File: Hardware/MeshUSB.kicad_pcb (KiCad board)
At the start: 2 copper layers, 30.2 x 44.3 mm, 42 parts, among them P1 USB_4, P2 PVCell, Q1 MOS_P, U1 XBEE, U2 AP7313-3.3VREGULATOR, U4 FT231X-SSOP, U5 LTC4070

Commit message: Begin major modifications for post v0.2.
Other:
- board text added: "MeshUSBv0.3"
- board text removed: "MeshUSBv0.2"

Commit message: Begin Layout. Still some schematic additions required.
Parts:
- removed C1: 10uF, _MUSB_SM0603_Capa
- removed D3, D4: DIODE-NC, SOT23
- removed R3, R6: 22R, _MUSB_SM0603_Resistor
- added C30: 100n, _MUSB_:_MUSB_SM0603_Capa, F.Cu at (165.3, 137.1)
- added D30: BAT54C, SMD_Packages:SOT23, F.Cu at (170.4, 133.4)
- added R30: 10R, _MUSB_:_MUSB_SM0603_Resistor, F.Cu at (170.0, 128.6)
- moved G0 6.98 mm to (138.5, 93.7)
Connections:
- D7 pad 1: N-0000032 -> Net-(C30-Pad1)
- Li-Battery1 pad 1: N-0000032 -> Net-(C30-Pad1)
- Q1 pad 2: N-0000032 -> Net-(C30-Pad1)
- U5 pad 2: N-0000032 -> Net-(C30-Pad1)
- U5 pad 3: N-0000032 -> Net-(U5-Pad3)
- U5 pad 8: N-0000032 -> Net-(C30-Pad1)
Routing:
- net GND: track 112.3 -> 0.00 mm, vias 3 -> 0
- net N-0000032: track 78.6 -> 0.00 mm, vias 3 -> 0
- net USB_VDD: track 45.6 -> 0.00 mm
- net Net-(D2-Pad2): track 39.7 -> 0.00 mm, vias 2 -> 0
- net _MT_PF2: track 33.1 -> 0.00 mm, vias 2 -> 0
- net Net-(P1-Pad3): track 31.1 -> 0.00 mm, vias 2 -> 0
- net Net-(H1-Pad3): track 28.0 -> 0.00 mm, vias 2 -> 0
- net Net-(D1-Pad2): track 27.9 -> 0.00 mm
- net _MT_PF3: track 27.1 -> 0.00 mm, vias 2 -> 0
- net Net-(P1-Pad2): track 20.0 -> 0.00 mm
- net Net-(H1-Pad2): track 17.4 -> 0.00 mm
- net VCCIO: track 17.3 -> 0.00 mm
- net BAT+: track 16.5 -> 0.00 mm
- net N-0000035: track 16.4 -> 0.00 mm
- net Net-(R1-Pad2): track 15.2 -> 0.00 mm
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
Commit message: Further changes. Still looking for appropriate diode and PMOS packages.
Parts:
- moved R30 29.4 mm to (143.2, 116.6), turned to 180 degrees
- moved D30 26.8 mm to (154.0, 112.2)
- moved C30 25.0 mm to (153.9, 114.9), turned to 180 degrees
- moved U2 5.89 mm to (143.4, 108.0)
- moved R4 3.10 mm to (149.2, 109.0)
- moved JP2 2.05 mm to (146.4, 108.3), turned to 0 degrees
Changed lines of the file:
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@@
   )
   (module SOT23 (layer F.Cu)
-    (at 148.5 110.88 180)
+    (at 143.36 108 180)
     (tags SOT23)
     (fp_text reference U2 (at 1.99898 -0.09906 270) (layer F.SilkS)
@@
   )
   (module _MUSB_SM0603_Resistor (layer F.Cu)
-    (at 146.07 109.09 90)
+    (at 149.17 109.04 90)
     (attr smd)
     (fp_text reference R4 (at -0.762 0 180) (layer F.SilkS)
@@
   )
   (module _MUSB_SMTJumper (layer F.Cu)
-    (at 148.5 108.32 180)
-    (attr smd)
-    (fp_text reference JP2 (at -0.74 0 270) (layer F.SilkS)
+    (at 146.45 108.28)
+    (attr smd)
+    (fp_text reference JP2 (at -0.74 0 90) (layer F.SilkS)
       (effects (font (size 0.2 0.2) (thickness 0.05)))
     )
-    (fp_text value JUMPER (at 0 0 180) (layer F.SilkS) hide
+    (fp_text value JUMPER (at 0 0) (layer F.SilkS) hide
       (effects (font (size 0.508 0.4572) (thickness 0.1143)))
     )
-    (pad 1 smd rect (at -0.65 0 180) (size 0.5 0.9) (layers F.Cu F.Paste F.Mask)
+    (pad 1 smd rect (at -0.65 0) (size 0.5 0.9) (layers F.Cu F.Paste F.Mask)
       (net 32 "Net-(JP2-Pad1)"))
-    (pad 2 smd rect (at 0.65 0 180) (size 0.5 0.9) (layers F.Cu F.Paste F.Mask)
+    (pad 2 smd rect (at 0.65 0) (size 0.5 0.9) (layers F.Cu F.Paste F.Mask)
       (net 33 "Net-(JP2-Pad2)"))
-    (pad 2 smd rect (at 0 0 180) (size 1.5 0.2032) (layers F.Cu F.Paste F.Mask)
+    (pad 2 smd rect (at 0 0) (size 1.5 0.2032) (layers F.Cu F.Paste F.Mask)
       (net 33 "Net-(JP2-Pad2)"))
     (model smd\resistors\R0603.wrl
@@
   )
   (module _MUSB_:_MUSB_SM0603_Capa (layer F.Cu)
-    (at 165.35 137.13)
-    (attr smd)
-    (fp_text reference C30 (at -0.8 0 90) (layer F.SilkS)
-      (effects (font (size 0.35 0.35) (thickness 0.0875)))
-    )
-    (fp_text value 100n (at 0.8 0 90) (layer F.SilkS)
-      (effects (font (size 0.35 0.35) (thickness 0.0875)))
-    )
-    (fp_text user "" (at -0.8 0 90) (layer F.SilkS)
+    (at 153.88 114.93 180)
+    (attr smd)
+    (fp_text reference C30 (at -0.8 0 270) (layer F.SilkS)
+      (effects (font (size 0.35 0.35) (thickness 0.0875)))
+    )
+    (fp_text value 100n (at 0.8 0 270) (layer F.SilkS)
+      (effects (font (size 0.35 0.35) (thickness 0.0875)))
+    )
+    (fp_text user "" (at -0.8 0 270) (layer F.SilkS)
       (effects (font (size 0.35 0.35) (thickness 0.0875)))
     )
@@
     (fp_line (start 1.19888 -0.635) (end 1.19888 0.635) (layer F.SilkS) (width 0.11938))
     (fp_line (start -1.19888 0.635) (end -1.19888 -0.635) (layer F.SilkS) (width 0.11938))
-    (pad 1 smd rect (at -0.762 0) (size 0.635 1.143) (layers F.Cu F.Paste F.Mask)
+    (pad 1 smd rect (at -0.762 0 180) (size 0.635 1.143) (layers F.Cu F.Paste F.Mask)
       (net 3 "Net-(C30-Pad1)"))
-    (pad 2 smd rect (at 0.762 0) (size 0.635 1.143) (layers F.Cu F.Paste F.Mask)
+    (pad 2 smd rect (at 0.762 0 180) (size 0.635 1.143) (layers F.Cu F.Paste F.Mask)
       (net 2 GND))
     (model smd\capacitors\C0603.wrl
@@
   )
   (module SMD_Packages:SOT23 (layer F.Cu)
-    (at 170.38 133.44)
+    (at 154 112.22)
     (tags SOT23)
     (fp_text reference D30 (at 1.99898 -0.09906 90) (layer F.SilkS)
@@
   )
   (module _MUSB_:_MUSB_SM0603_Resistor (layer F.Cu)
-    (at 170.04 128.64)
-    (attr smd)
-    (fp_text reference R30 (at -0.762 0 90) (layer F.SilkS)
-      (effects (font (size 0.35 0.35) (thickness 0.0875)))
-    )
-    (fp_text value 10R (at 0.762 0 90) (layer F.SilkS)
+    (at 143.16 116.63 180)
+    (attr smd)
+    (fp_text reference R30 (at -0.762 0 270) (layer F.SilkS)
+      (effects (font (size 0.35 0.35) (thickness 0.0875)))
+    )
+    (fp_text value 10R (at 0.762 0 270) (layer F.SilkS)
       (effects (font (size 0.35 0.35) (thickness 0.0875)))
     )
@@
     (fp_line (start 1.2065 -0.6985) (end 1.2065 0.6985) (layer F.SilkS) (width 0.127))
     (fp_line (start 1.2065 0.6985) (end 0.50038 0.6985) (layer F.SilkS) (width 0.127))
-    (pad 1 smd rect (at -0.762 0) (size 0.635 1.143) (layers F.Cu F.Paste F.Mask)
+    (pad 1 smd rect (at -0.762 0 180) (size 0.635 1.143) (layers F.Cu F.Paste F.Mask)
       (net 11 "Net-(D30-Pad3)"))
-    (pad 2 smd rect (at 0.762 0) (size 0.635 1.143) (layers F.Cu F.Paste F.Mask)
+    (pad 2 smd rect (at 0.762 0 180) (size 0.635 1.143) (layers F.Cu F.Paste F.Mask)
       (net 3 "Net-(C30-Pad1)"))
     (model smd\resistors\R0603.wrl
@@
     (effects (font (size 0.5 0.5) (thickness 0.125)))
   )
-  (gr_text "V.Div.\nJPR" (at 148.5 106.84) (layer F.SilkS)
+  (gr_text "V.Div.\nJPR" (at 146.38 107.02) (layer F.SilkS)
     (effects (font (size 0.45 0.45) (thickness 0.1125)))
   )

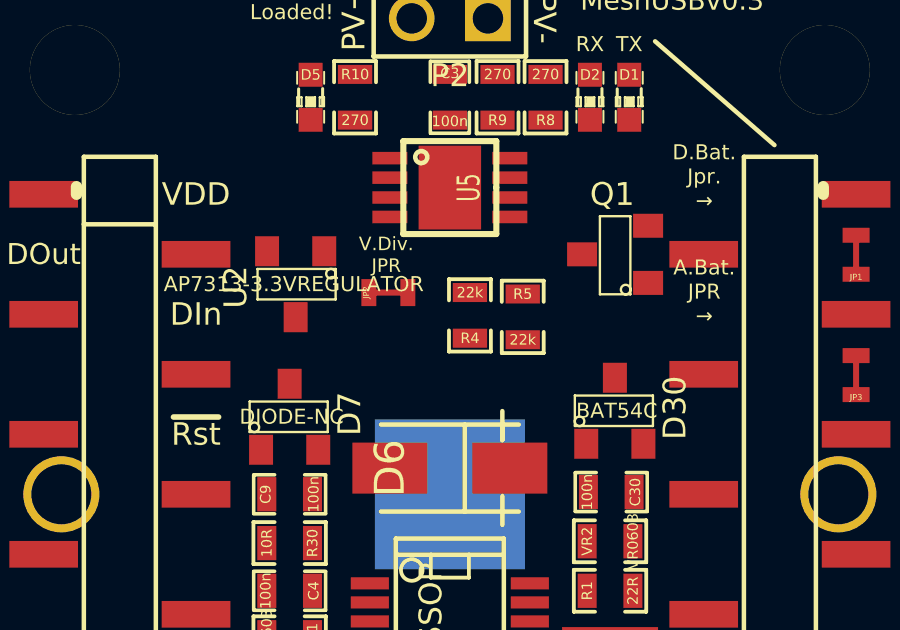
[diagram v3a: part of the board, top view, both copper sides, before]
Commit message: Schematic notes and library updates.
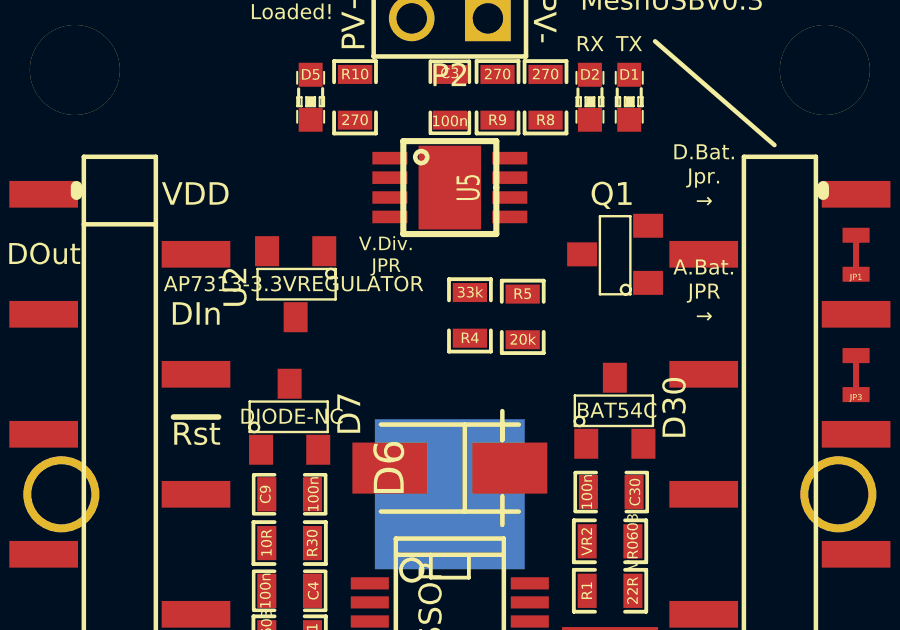
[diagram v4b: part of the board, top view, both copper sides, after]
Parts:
- removed JP2: JUMPER, _MUSB_SMTJumper
- R4: value 22k -> 33k
- R5: value 22k -> 20k
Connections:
- Q1 pad 3: Net-(JP2-Pad1) -> Net-(Q1-Pad3)
- R4 pad 2: Net-(JP2-Pad2) -> Net-(Q1-Pad3)
- R5 pad 2: GND -> _MT_PE4
- U2 pad 1: Net-(JP2-Pad1) -> Net-(Q1-Pad3)

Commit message: Almost to layout. Charging slightly modified, confirming BOM.
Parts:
- added JP2: CONN_TH_JMPR_DEFAULTCLOSED, _MUSB_SMTJumper, F.Cu at (169.8, 116.0)
- added Q2: MOS_P-INFINEON-BSS83P, SMD_Packages:SOT23, F.Cu at (146.8, 109.7)
- D30: value BAT54C -> DUAL_SHOTTKEY_PACKAGE
- R30: value 10R -> 16R; footprint _MUSB_:_MUSB_SM0603_Resistor -> SMD_Packages:SM2512
- moved R30 25.7 mm to (148.1, 91.4), turned to 0 degrees
- moved R5 7.28 mm to (156.6, 104.5), turned to 0 degrees
- moved R4 6.61 mm to (153.9, 104.4), turned to 180 degrees
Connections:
- H1 pad 5: Net-(C9-Pad1) -> Net-(H1-Pad5)

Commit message: Layoutsplosion.
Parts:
- added JP4: JUMPER, _MUSB_:_MUSB_SMTJumper, F.Cu at (162.1, 122.9)
- added P30: JST_2, _MUSB_:_MUSB_JST-2mm-THs, F.Cu at (148.5, 100.0)
- JP2: footprint _MUSB_SMTJumper -> _MUSB_:_MUSB_TH-Jumper_Default-Connected
- U1: footprint _MUSB_XBee_Board_OUTLINE_ONLY -> _MUSB_:_MUSB_XBee_Board_OUTLINE_ONLY
- moved R4 34.3 mm to (168.9, 135.3), turned to 90 degrees
- moved R5 33.8 mm to (170.4, 135.3), turned to 90 degrees
- moved JP2 30.4 mm to (141.0, 125.7)
- moved D2 27.8 mm to (143.1, 127.7), turned to 90 degrees
- moved R9 26.5 mm to (144.7, 127.8), turned to 270 degrees
- moved R8 26.0 mm to (152.2, 127.8), turned to 270 degrees
- moved D1 26.0 mm to (153.7, 127.8), turned to 90 degrees
- moved G1 20.6 mm to (169.0, 130.0)
- moved C3 17.2 mm to (156.4, 117.0), turned to 90 degrees
- moved R30 12.6 mm to (148.5, 104.0), turned to 180 degrees
- moved F1 7.64 mm to (148.5, 127.8), turned to 0 degrees
- moved P2 7.07 mm to (155.5, 100.0), turned to 0 degrees
- moved U5 6.72 mm to (148.5, 111.5)
- moved Q1 5.09 mm to (154.0, 112.1), turned to 0 degrees
- moved D30 4.12 mm to (154.0, 108.1), turned to 180 degrees
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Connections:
- JP2 pad 2: (no net) -> Net-(H1-Pad5)
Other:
- board text added: "PE4 JPR"
- board text added: "©BobPowers 2014 OpenHardware Under TAPR OHL tapr.org/OHL"
- board text removed: "V.Div. JPR"
- board text removed: "©BobPowers 2013 OpenHardware Under TAPR OHL tapr.org/OHL"

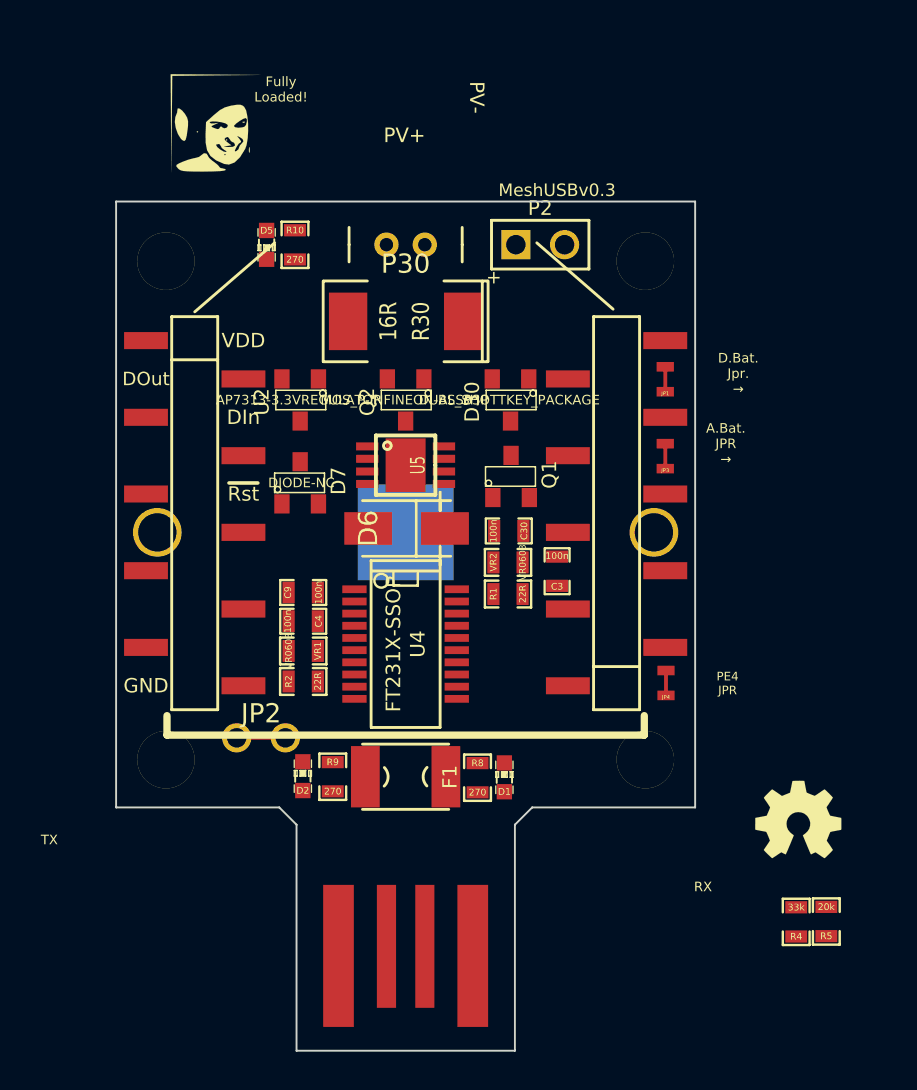
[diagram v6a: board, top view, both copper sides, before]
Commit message: Layout positions nearly finalized.
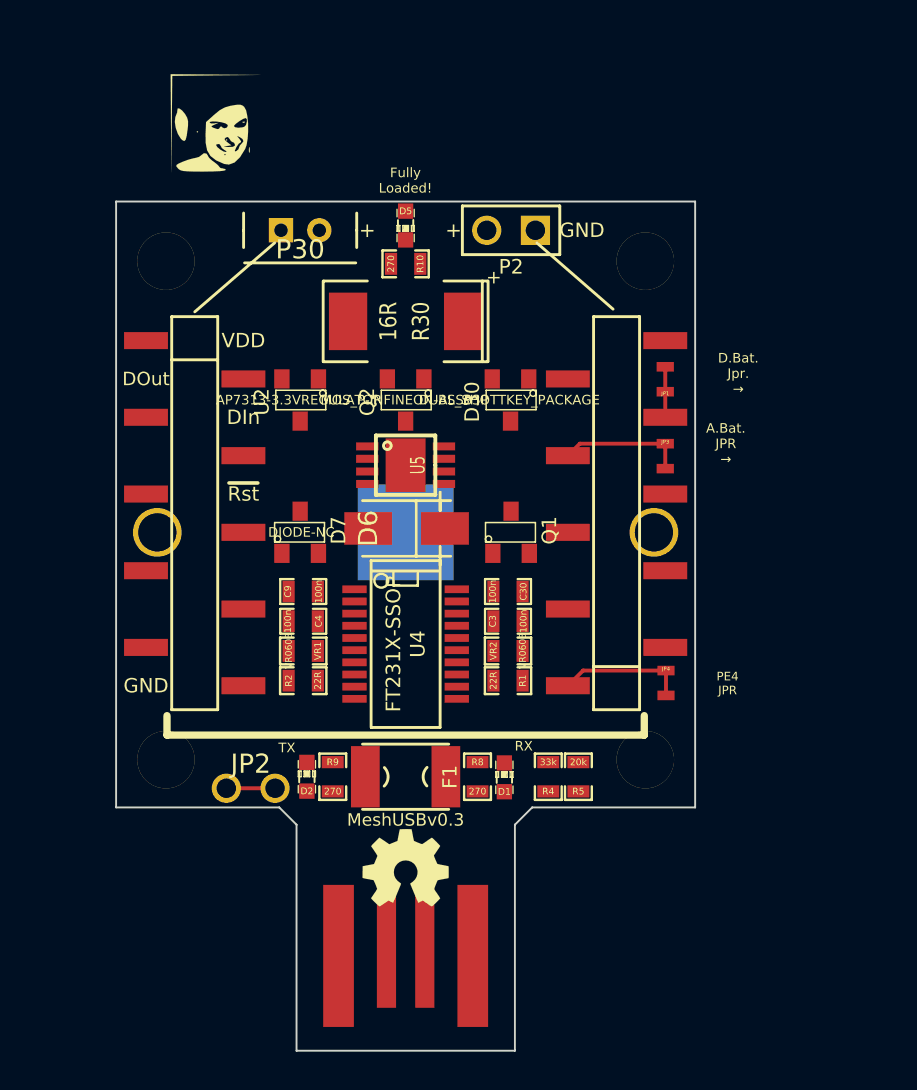
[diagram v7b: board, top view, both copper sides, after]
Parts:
- 1PIN4: footprint _MUSB_3mmTH-1pin -> _MUSB_:_MUSB_3mmTH-1pin
- moved G1 20.6 mm to (148.5, 132.5)
- moved R4 15.0 mm to (155.9, 127.8)
- moved R5 15.0 mm to (157.5, 127.8)
- moved D5 7.32 mm to (148.5, 99.0)
- moved R10 5.85 mm to (148.5, 101.0), turned to 180 degrees
- moved P30 5.55 mm to (143.0, 99.2)
- moved VR2 4.62 mm to (153.8, 121.2)
- moved R1 4.52 mm to (153.8, 122.7), turned to 180 degrees
- moved C3 3.66 mm to (153.8, 119.6), turned to 0 degrees
- moved C30 3.16 mm to (153.8, 118.1)
- moved Q1 2.91 mm to (154.0, 115.0)
- moved JP2 2.68 mm to (140.4, 128.3)
- moved D7 2.58 mm to (143.0, 115.0)
- moved P2 1.69 mm to (154.0, 99.2), turned to 180 degrees
- moved 1PIN4 0.22 mm to (161.0, 126.9)
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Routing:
- net Net-(H2-Pad1): track 0.00 -> 5.45 mm
- net Net-(H2-Pad7): track 0.00 -> 5.34 mm
- net _MT_PF2: track 0.00 -> 1.33 mm
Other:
- board text added: "+"
- board text removed: "PV+"
- board text removed: "PV-"

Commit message: Further placements, silks, refs. Next:Double check all pins and packages.
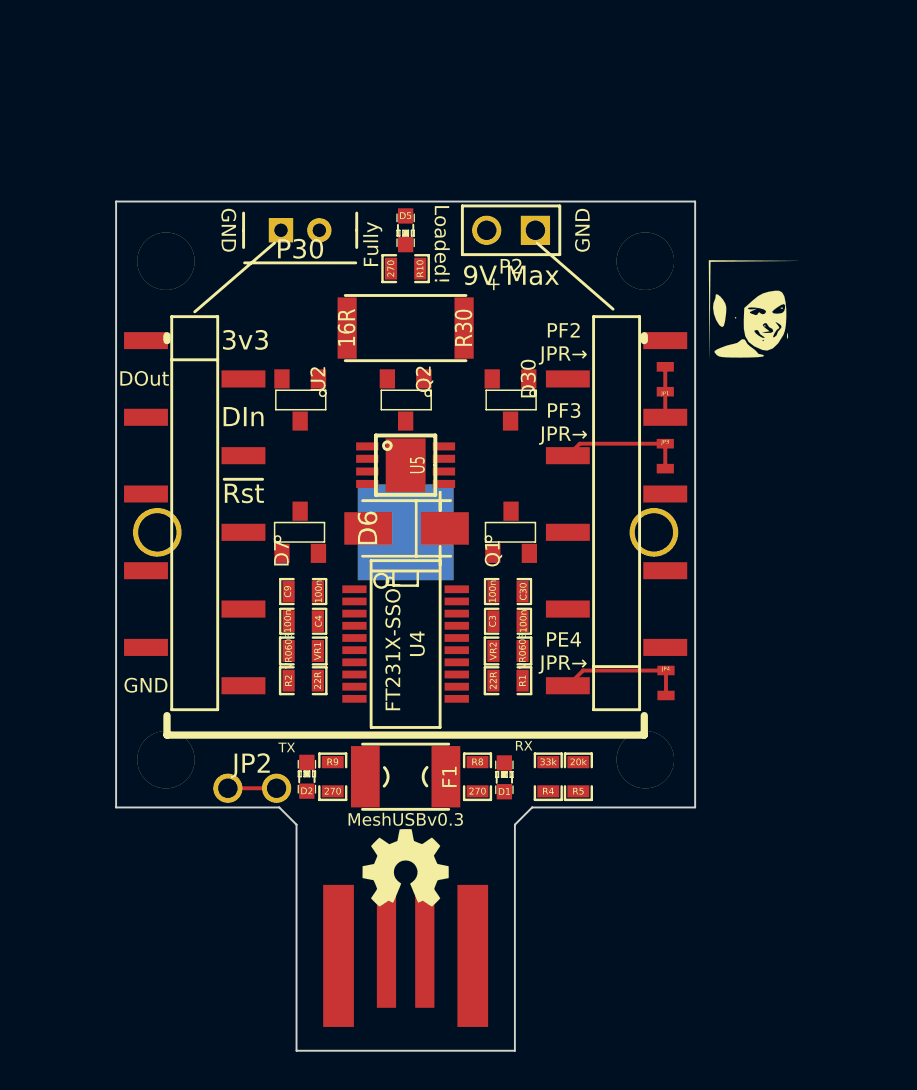
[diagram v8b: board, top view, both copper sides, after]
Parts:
- D30, Q2: footprint SMD_Packages:SOT23 -> _MUSB_:_MUSB_SOT23
- D7, Q1, U2: footprint SOT23 -> _MUSB_:_MUSB_SOT23
- JP3: footprint _MUSB_SMTJumper -> _MUSB_:_MUSB_SMTJumper
- R30: footprint SMD_Packages:SM2512 -> _MUSB_:_MUSB_TE3521-Series_Resistor-6.3x3.2
- U1: footprint _MUSB_:_MUSB_XBee_Board_OUTLINE_ONLY -> _MUSB_XBee_Board_OUTLINE_ONLY
- moved G0 29.7 mm to (166.6, 103.3)
- moved R30 0.35 mm to (148.5, 104.3)
- moved D5 0.25 mm to (148.5, 99.2)
- moved R10 0.25 mm to (148.5, 101.2)
- moved JP2 0.08 mm to (140.5, 128.3)
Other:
- board text added: "3v3"
- board text added: "9V Max"
- board text added: "Fully"
- board text added: "Loaded!"
- board text added: "PE4 JPR→"
- board text added: "PF2 JPR→"
- board text added: "PF3 JPR→"
- board text added: "©BobPowers 2013 OpenHardware Under TAPR OHL tapr.org/OHL"
- board text removed: "+"
- board text removed: "A.Bat. JPR →"
- board text removed: "D.Bat. Jpr. →"
- board text removed: "Fully Loaded!"
- board text removed: "PE4 JPR"
- board text removed: "VDD"
- board text removed: "©BobPowers 2014 OpenHardware Under TAPR OHL tapr.org/OHL"
